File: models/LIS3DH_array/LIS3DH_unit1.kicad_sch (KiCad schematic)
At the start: 8 parts, among them J1 Conn_01x08_Socket, U1 LIS3DH

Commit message: updated LIS3DH array
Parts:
- renumbered C1 to C17, C2 to C18, J1 to J14, TP1 to TP41, TP10 to TP42, TP19 to TP43, TP28 to TP44, U1 to U11
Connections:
- net GND: now also J14.1 (Pin_1), U11.10 (RES), U11.12 (GND); no longer J14.2 (Pin_2)
- net SCLK_SCL: now also J14.2 (Pin_2); no longer J14.5 (Pin_5)
- net SDI_SDA: now also J14.3 (Pin_3); no longer J14.4 (Pin_4)
- net SDO_ADDR: now also J14.4 (Pin_4); no longer J14.6 (Pin_6)
- net VDD: now also J14.6 (Pin_6); no longer J14.1 (Pin_1)
- net nCS: now also J14.5 (Pin_5); no longer J14.3 (Pin_3)

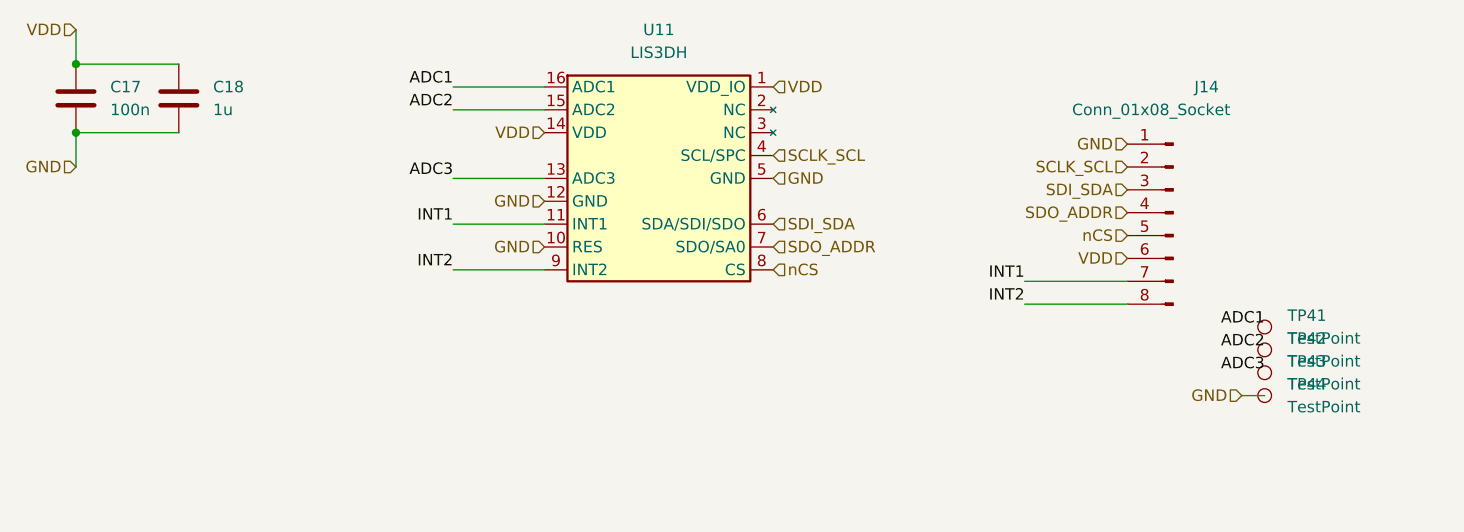
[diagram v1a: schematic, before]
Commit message: updated lis3dh array: fpc connectors
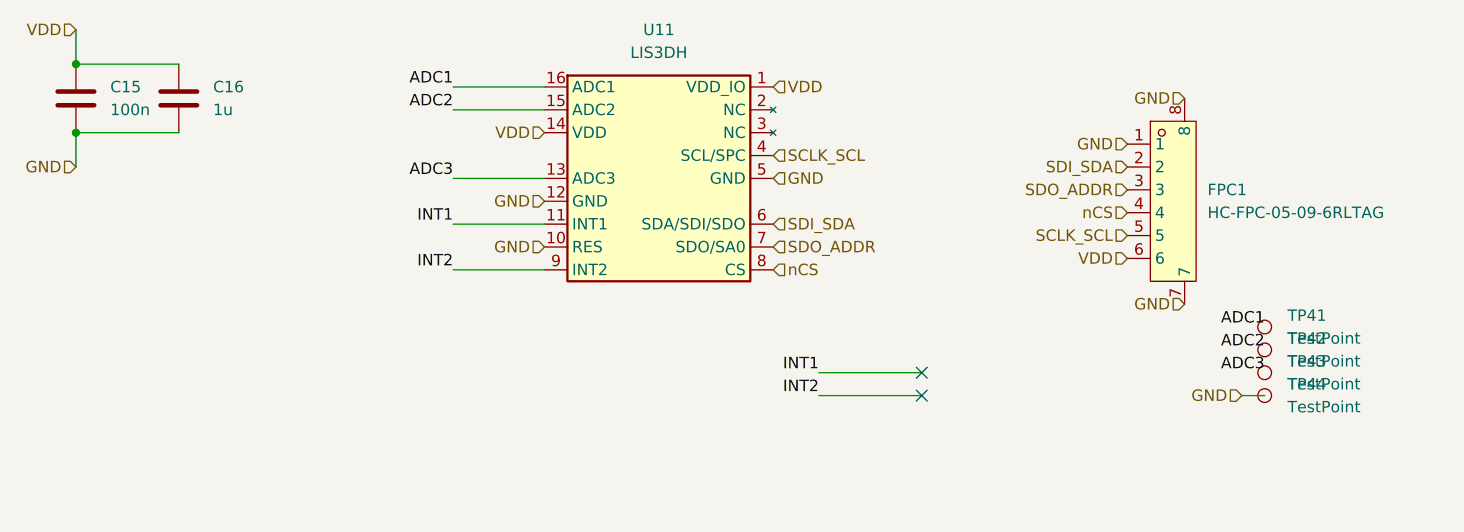
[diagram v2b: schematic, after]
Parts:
- removed J14: Conn_01x08_Socket, Connector_PinSocket_1.27mm:PinSocket_1x08_P1.27mm_Vertical, symbol Connector:Conn_01x08_Pin
- added FPC1: HC-FPC-05-09-6RLTAG, 00_lcsc:FPC-SMD_6P-P0.50_HC-FPC-05-09-6RLTAG, symbol 00_lcsc:HC-FPC-05-09-6RLTAG
- C15: renamed from C17; footprint Capacitor_SMD:C_01005_0402Metric -> Capacitor_SMD:C_0402_1005Metric_Pad0.74x0.62mm_HandSolder
- C16: renamed from C18; footprint Capacitor_SMD:C_01005_0402Metric -> Capacitor_SMD:C_0402_1005Metric_Pad0.74x0.62mm_HandSolder
- U11: footprint Package_LGA:LGA-16_3x3mm_P0.5mm_LayoutBorder3x5y -> 00_custom-footprints:LGA-16_3x3mm_P0.5mm_LayoutBorder3x5y
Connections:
- net GND: now also FPC1.1, FPC1.7, FPC1.8
- net SCLK_SCL: now also FPC1.5
- net SDI_SDA: now also FPC1.2
- net SDO_ADDR: now also FPC1.3
- net VDD: now also FPC1.6
- net nCS: now also FPC1.4
- no-connect marks 0 -> 2

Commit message: updated
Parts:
- TP41, TP42, TP43, TP44: now left out of the parts list
- renumbered C15 to C17, C16 to C18
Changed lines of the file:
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@@
 		(unit 1)
 		(exclude_from_sim no)
-		(in_bom yes)
+		(in_bom no)
 		(on_board yes)
 		(dnp no)
@@
 		(unit 1)
 		(exclude_from_sim no)
-		(in_bom yes)
+		(in_bom no)
 		(on_board yes)
 		(dnp no)
@@
 		(dnp no)
 		(fields_autoplaced yes)
-		(property "Reference" "C16"
+		(property "Reference" "C18"
 			(at 80.01 81.2799 0)
 			(effects
@@
 		(instances
 			(project "LIS3DH_array"
+				(path "/088343b1-32aa-43c7-a40d-604456041856/0a250753-2f1b-4db6-b0fd-bb786fbfaec2"
+					(reference "C18")
+					(unit 1)
+				)
+				(path "/088343b1-32aa-43c7-a40d-604456041856/6ff9cbdb-1f0b-4509-9e89-28e95e7baab2"
+					(reference "C32")
+					(unit 1)
+				)
+				(path "/088343b1-32aa-43c7-a40d-604456041856/ef86a211-0e67-48a9-a57b-8c0dad3edc25"
+					(reference "C30")
+					(unit 1)
+				)
+				(path "/088343b1-32aa-43c7-a40d-604456041856/4196b40b-41a0-4a32-a0e5-7d2da09f4f78"
+					(reference "C28")
+					(unit 1)
+				)
+				(path "/088343b1-32aa-43c7-a40d-604456041856/99abc178-3461-4064-878a-d14b9aa8e7b1"
+					(reference "C26")
+					(unit 1)
+				)
+				(path "/088343b1-32aa-43c7-a40d-604456041856/c0533eda-3faa-4178-be48-87706e607a8a"
+					(reference "C6")
+					(unit 1)
+				)
+				(path "/088343b1-32aa-43c7-a40d-604456041856/a04c0eda-47a2-46bc-985a-c37d56d9cb86"
+					(reference "C12")
+					(unit 1)
+				)
+				(path "/088343b1-32aa-43c7-a40d-604456041856/449a3e28-5934-4b78-90c2-2442296ef97e"
+					(reference "C8")
+					(unit 1)
+				)
+				(path "/088343b1-32aa-43c7-a40d-604456041856/46bbfefa-b39d-49c9-9b2f-2fb0dc009f69"
+					(reference "C10")
+					(unit 1)
+				)
+				(path "/088343b1-32aa-43c7-a40d-604456041856/6a21ef4e-4a58-4190-875b-67aaaf15cc55"
+					(reference "C4")
+					(unit 1)
+				)
+				(path "/088343b1-32aa-43c7-a40d-604456041856/fab6b3a9-ce82-4557-b47a-fa6fff2ead3c"
+					(reference "C14")
+					(unit 1)
+				)
+				(path "/088343b1-32aa-43c7-a40d-604456041856/b19dac12-c9b9-47a0-bceb-0440011a6691"
+					(reference "C2")
+					(unit 1)
+				)
+				(path "/088343b1-32aa-43c7-a40d-604456041856/4b16ea52-b402-4508-92b9-7a07f8adf659"
+					(reference "C20")
+					(unit 1)
+				)
+				(path "/088343b1-32aa-43c7-a40d-604456041856/216bdaa4-b21c-4fea-a134-fc9e53e2c5be"
+					(reference "C22")
+					(unit 1)
+				)
+				(path "/088343b1-32aa-43c7-a40d-604456041856/4efa5324-09d0-404b-8518-dd309e1a12de"
+					(reference "C24")
+					(unit 1)
+				)
 				(path "/088343b1-32aa-43c7-a40d-604456041856/f976a518-1256-4c19-93c6-910baefe5403"
 					(reference "C16")
-					(unit 1)
-				)
-				(path "/088343b1-32aa-43c7-a40d-604456041856/0a250753-2f1b-4db6-b0fd-bb786fbfaec2"
-					(reference "C18")
-					(unit 1)
-				)
-				(path "/088343b1-32aa-43c7-a40d-604456041856/4efa5324-09d0-404b-8518-dd309e1a12de"
-					(reference "C24")
-					(unit 1)
-				)
-				(path "/088343b1-32aa-43c7-a40d-604456041856/216bdaa4-b21c-4fea-a134-fc9e53e2c5be"
-					(reference "C22")
-					(unit 1)
-				)
-				(path "/088343b1-32aa-43c7-a40d-604456041856/4b16ea52-b402-4508-92b9-7a07f8adf659"
-					(reference "C20")
-					(unit 1)
-				)
-				(path "/088343b1-32aa-43c7-a40d-604456041856/b19dac12-c9b9-47a0-bceb-0440011a6691"
-					(reference "C2")
-					(unit 1)
-				)
-				(path "/088343b1-32aa-43c7-a40d-604456041856/fab6b3a9-ce82-4557-b47a-fa6fff2ead3c"
-					(reference "C14")
-					(unit 1)
-				)
-				(path "/088343b1-32aa-43c7-a40d-604456041856/6a21ef4e-4a58-4190-875b-67aaaf15cc55"
-					(reference "C4")
-					(unit 1)
-				)
-				(path "/088343b1-32aa-43c7-a40d-604456041856/46bbfefa-b39d-49c9-9b2f-2fb0dc009f69"
-					(reference "C10")
-					(unit 1)
-				)
-				(path "/088343b1-32aa-43c7-a40d-604456041856/449a3e28-5934-4b78-90c2-2442296ef97e"
-					(reference "C8")
-					(unit 1)
-				)
-				(path "/088343b1-32aa-43c7-a40d-604456041856/a04c0eda-47a2-46bc-985a-c37d56d9cb86"
-					(reference "C12")
-					(unit 1)
-				)
-				(path "/088343b1-32aa-43c7-a40d-604456041856/c0533eda-3faa-4178-be48-87706e607a8a"
-					(reference "C6")
-					(unit 1)
-				)
-				(path "/088343b1-32aa-43c7-a40d-604456041856/99abc178-3461-4064-878a-d14b9aa8e7b1"
-					(reference "C26")
-					(unit 1)
-				)
-				(path "/088343b1-32aa-43c7-a40d-604456041856/4196b40b-41a0-4a32-a0e5-7d2da09f4f78"
-					(reference "C28")
-					(unit 1)
-				)
-				(path "/088343b1-32aa-43c7-a40d-604456041856/ef86a211-0e67-48a9-a57b-8c0dad3edc25"
-					(reference "C30")
-					(unit 1)
-				)
-				(path "/088343b1-32aa-43c7-a40d-604456041856/6ff9cbdb-1f0b-4509-9e89-28e95e7baab2"
-					(reference "C32")
 					(unit 1)
 				)
@@
 		(dnp no)
 		(fields_autoplaced yes)
-		(property "Reference" "C15"
+		(property "Reference" "C17"
 			(at 68.58 81.2799 0)
 			(effects
@@
 		(instances
 			(project "LIS3DH_array"
+				(path "/088343b1-32aa-43c7-a40d-604456041856/0a250753-2f1b-4db6-b0fd-bb786fbfaec2"
+					(reference "C17")
+					(unit 1)
+				)
+				(path "/088343b1-32aa-43c7-a40d-604456041856/6ff9cbdb-1f0b-4509-9e89-28e95e7baab2"
+					(reference "C31")
+					(unit 1)
+				)
+				(path "/088343b1-32aa-43c7-a40d-604456041856/ef86a211-0e67-48a9-a57b-8c0dad3edc25"
+					(reference "C29")
+					(unit 1)
+				)
+				(path "/088343b1-32aa-43c7-a40d-604456041856/4196b40b-41a0-4a32-a0e5-7d2da09f4f78"
+					(reference "C27")
+					(unit 1)
+				)
+				(path "/088343b1-32aa-43c7-a40d-604456041856/99abc178-3461-4064-878a-d14b9aa8e7b1"
+					(reference "C25")
+					(unit 1)
+				)
+				(path "/088343b1-32aa-43c7-a40d-604456041856/c0533eda-3faa-4178-be48-87706e607a8a"
+					(reference "C5")
+					(unit 1)
+				)
+				(path "/088343b1-32aa-43c7-a40d-604456041856/a04c0eda-47a2-46bc-985a-c37d56d9cb86"
+					(reference "C11")
+					(unit 1)
+				)
+				(path "/088343b1-32aa-43c7-a40d-604456041856/449a3e28-5934-4b78-90c2-2442296ef97e"
+					(reference "C7")
+					(unit 1)
+				)
+				(path "/088343b1-32aa-43c7-a40d-604456041856/46bbfefa-b39d-49c9-9b2f-2fb0dc009f69"
+					(reference "C9")
+					(unit 1)
+				)
+				(path "/088343b1-32aa-43c7-a40d-604456041856/6a21ef4e-4a58-4190-875b-67aaaf15cc55"
+					(reference "C3")
+					(unit 1)
+				)
+				(path "/088343b1-32aa-43c7-a40d-604456041856/fab6b3a9-ce82-4557-b47a-fa6fff2ead3c"
+					(reference "C13")
+					(unit 1)
+				)
+				(path "/088343b1-32aa-43c7-a40d-604456041856/b19dac12-c9b9-47a0-bceb-0440011a6691"
+					(reference "C1")
+					(unit 1)
+				)
+				(path "/088343b1-32aa-43c7-a40d-604456041856/4b16ea52-b402-4508-92b9-7a07f8adf659"
+					(reference "C19")
+					(unit 1)
+				)
+				(path "/088343b1-32aa-43c7-a40d-604456041856/216bdaa4-b21c-4fea-a134-fc9e53e2c5be"
+					(reference "C21")
+					(unit 1)
+				)
+				(path "/088343b1-32aa-43c7-a40d-604456041856/4efa5324-09d0-404b-8518-dd309e1a12de"
+					(reference "C23")
+					(unit 1)
+				)
 				(path "/088343b1-32aa-43c7-a40d-604456041856/f976a518-1256-4c19-93c6-910baefe5403"
 					(reference "C15")
-					(unit 1)
-				)
-				(path "/088343b1-32aa-43c7-a40d-604456041856/0a250753-2f1b-4db6-b0fd-bb786fbfaec2"
-					(reference "C17")
-					(unit 1)
-				)
-				(path "/088343b1-32aa-43c7-a40d-604456041856/4efa5324-09d0-404b-8518-dd309e1a12de"
-					(reference "C23")
-					(unit 1)
-				)
-				(path "/088343b1-32aa-43c7-a40d-604456041856/216bdaa4-b21c-4fea-a134-fc9e53e2c5be"
-					(reference "C21")
-					(unit 1)
-				)
-				(path "/088343b1-32aa-43c7-a40d-604456041856/4b16ea52-b402-4508-92b9-7a07f8adf659"
-					(reference "C19")
-					(unit 1)
-				)
-				(path "/088343b1-32aa-43c7-a40d-604456041856/b19dac12-c9b9-47a0-bceb-0440011a6691"
-					(reference "C1")
-					(unit 1)
-				)
-				(path "/088343b1-32aa-43c7-a40d-604456041856/fab6b3a9-ce82-4557-b47a-fa6fff2ead3c"
-					(reference "C13")
-					(unit 1)
-				)
-				(path "/088343b1-32aa-43c7-a40d-604456041856/6a21ef4e-4a58-4190-875b-67aaaf15cc55"
-					(reference "C3")
-					(unit 1)
-				)
-				(path "/088343b1-32aa-43c7-a40d-604456041856/46bbfefa-b39d-49c9-9b2f-2fb0dc009f69"
-					(reference "C9")
-					(unit 1)
-				)
-				(path "/088343b1-32aa-43c7-a40d-604456041856/449a3e28-5934-4b78-90c2-2442296ef97e"
-					(reference "C7")
-					(unit 1)
-				)
-				(path "/088343b1-32aa-43c7-a40d-604456041856/a04c0eda-47a2-46bc-985a-c37d56d9cb86"
-					(reference "C11")
-					(unit 1)
-				)
-				(path "/088343b1-32aa-43c7-a40d-604456041856/c0533eda-3faa-4178-be48-87706e607a8a"
-					(reference "C5")
-					(unit 1)
-				)
-				(path "/088343b1-32aa-43c7-a40d-604456041856/99abc178-3461-4064-878a-d14b9aa8e7b1"
-					(reference "C25")
-					(unit 1)
-				)
-				(path "/088343b1-32aa-43c7-a40d-604456041856/4196b40b-41a0-4a32-a0e5-7d2da09f4f78"
-					(reference "C27")
-					(unit 1)
-				)
-				(path "/088343b1-32aa-43c7-a40d-604456041856/ef86a211-0e67-48a9-a57b-8c0dad3edc25"
-					(reference "C29")
-					(unit 1)
-				)
-				(path "/088343b1-32aa-43c7-a40d-604456041856/6ff9cbdb-1f0b-4509-9e89-28e95e7baab2"
-					(reference "C31")
 					(unit 1)
 				)
@@
 		(unit 1)
 		(exclude_from_sim no)
-		(in_bom yes)
+		(in_bom no)
 		(on_board yes)
 		(dnp no)
@@
 		(unit 1)
 		(exclude_from_sim no)
-		(in_bom yes)
+		(in_bom no)
 		(on_board yes)
 		(dnp no)

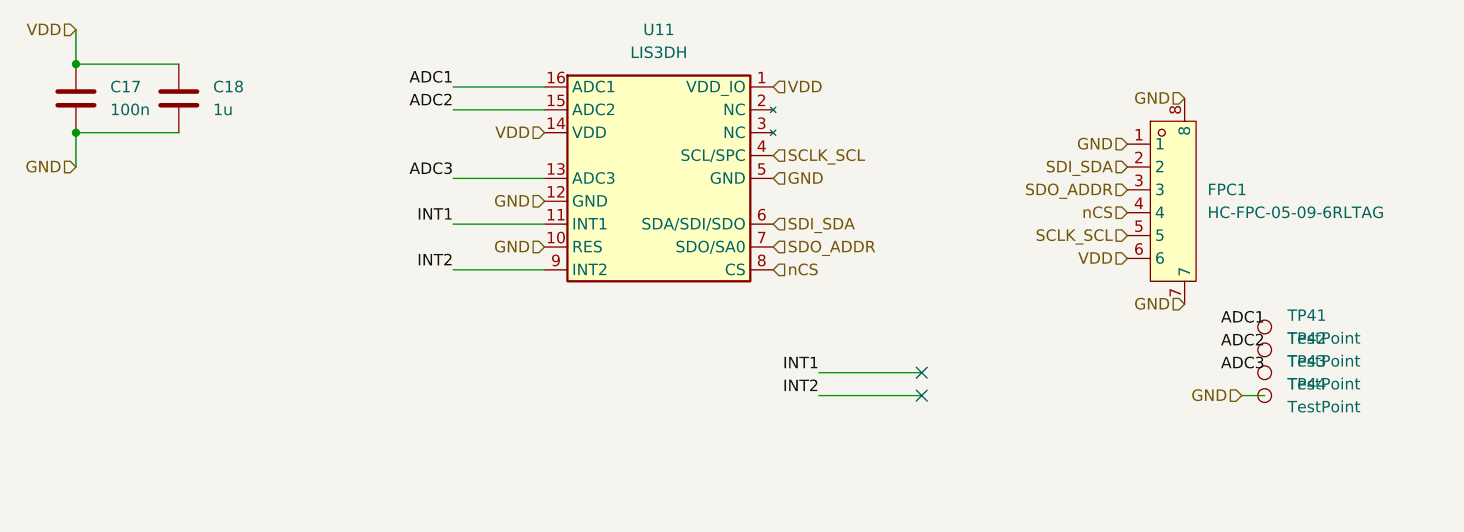
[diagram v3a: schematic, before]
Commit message: added or gate on each acc to prevent I2C interference when the chip have CSB high
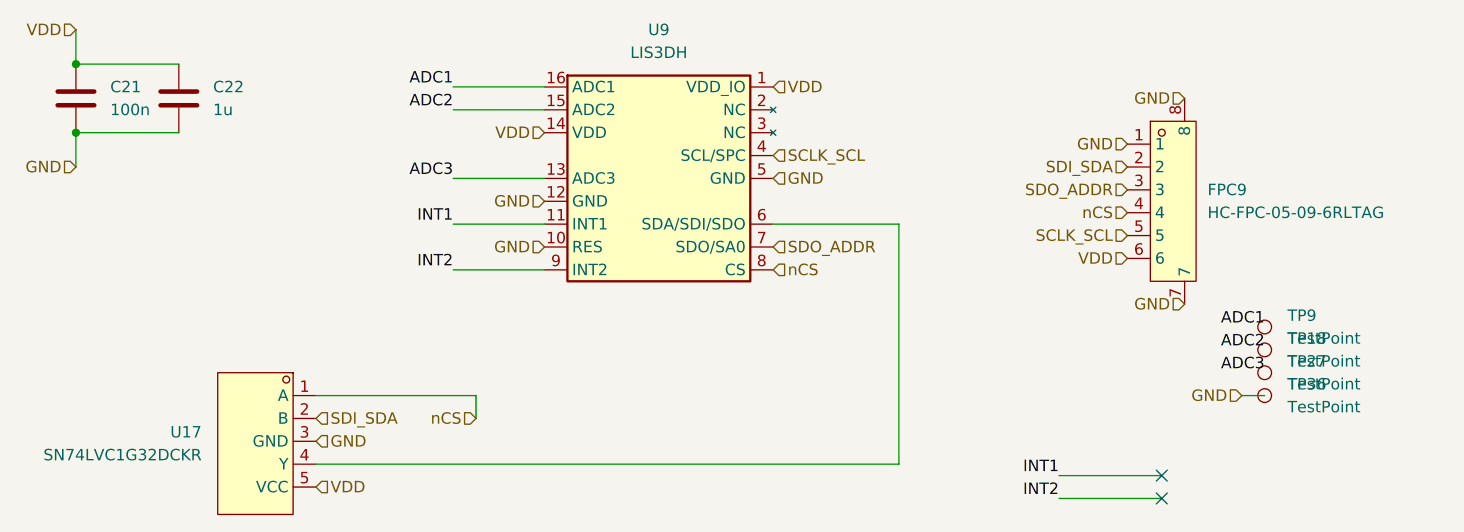
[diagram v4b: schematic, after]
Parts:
- added U17: SN74LVC1G32DCKR, 00_lcsc:SOT-353_L2.1-W1.3-P0.65-LS2.3-BR, symbol 00_lcsc:SN74LVC1G32DCKR
- renumbered C17 to C21, C18 to C22, FPC1 to FPC9, TP42 to TP18, TP43 to TP27, TP44 to TP36, TP41 to TP9, U11 to U9
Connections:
- net GND: now also U17.3 (GND)
- net SDI_SDA: now also U17.2 (B); no longer U9.6 (SDA/SDI/SDO)
- net VDD: now also U17.5 (VCC)
- net nCS: now also U17.1 (A)
- new net: U17.4 (Y), U9.6 (SDA/SDI/SDO)
